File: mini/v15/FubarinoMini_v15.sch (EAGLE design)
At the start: 35 parts, among them IC1 MCP1702T-3302E/MB, J1 M20, J2 M20, Q1 8MHz, Q2 32.768 KHz, U1 PIC32MX250F128D_44VTLA_44

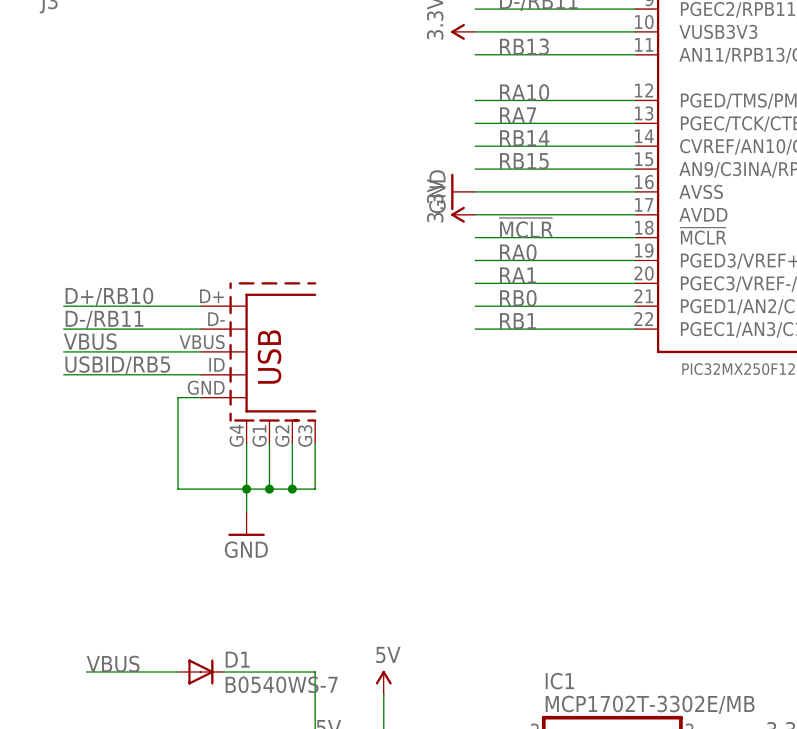
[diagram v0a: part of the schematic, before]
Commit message: "final" version 1.5 files, submitted to Microchip for their approval Updated USB connector footprint to Microchip's fav Hirose
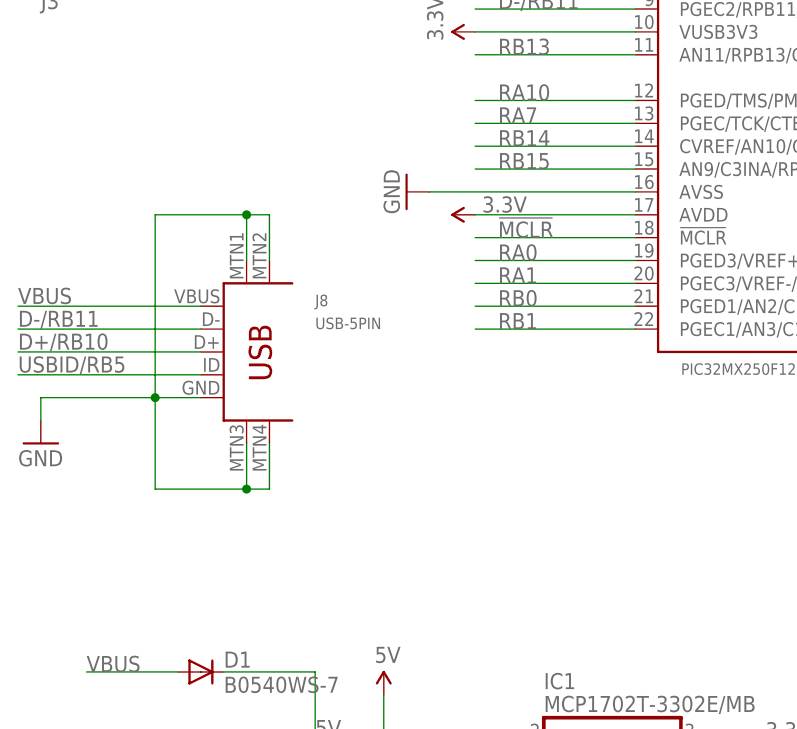
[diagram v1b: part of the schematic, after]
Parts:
- J8: value (none) -> USB-5PIN; device SparkFun02-20-08:USB_5PIN -> SchmalzHaus:USB-5PIN
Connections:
- net GND: now also J8.MTN1, J8.MTN2, J8.MTN3, J8.MTN4; no longer J8.P$1, J8.P$2, J8.P$3, J8.SHIELD
- net USBID/RB5: now also J8.ID; no longer J8.USB_ID
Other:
- note removed: "J8"
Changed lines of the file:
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@@
 <layer number="122" name="_bsilk" color="7" fill="1" visible="no" active="no"/>
 <layer number="125" name="_tNames" color="7" fill="1" visible="yes" active="yes"/>
+<layer number="128" name="128bmp" color="7" fill="1" visible="yes" active="yes"/>
+<layer number="129" name="129bmp" color="7" fill="1" visible="yes" active="yes"/>
+<layer number="130" name="130bmp" color="7" fill="1" visible="yes" active="yes"/>
 <layer number="144" name="Drill_legend" color="7" fill="1" visible="yes" active="yes"/>
 <layer number="151" name="HeatSink" color="7" fill="1" visible="no" active="no"/>
+<layer number="199" name="Contour" color="7" fill="1" visible="yes" active="yes"/>
 <layer number="200" name="200bmp" color="1" fill="10" visible="no" active="no"/>
 <layer number="201" name="201bmp" color="2" fill="1" visible="no" active="no"/>
@@
 <part name="GND8" library="SparkFun02-20-08" deviceset="GND" device=""/>
 <part name="FRAME2" library="SparkFun02-20-08" deviceset="FRAME-A3" device=""/>
-<part name="J8" library="SparkFun02-20-08" deviceset="USB_5PIN" device=""/>
 <part name="GND20" library="SparkFun02-20-08" deviceset="GND" device=""/>
 <part name="C13" library="SparkFun02-20-08" deviceset="CAP" device="0805" value="10uF"/>
@@
 <part name="U$3" library="SchmalzHausPublic" deviceset="ROSH_GARBAGE" device=""/>
 <part name="U$4" library="SchmalzHausPublic" deviceset="CHIPKIT" device="2MM"/>
+<part name="J8" library="SchmalzHaus" deviceset="USB-5PIN" device=""/>
 </parts>
 <sheets>
@@
 <plain>
 <text x="137.16" y="27.94" size="1.778" layer="98" rot="R90">Power ON LED</text>
-<text x="30.48" y="106.68" size="1.778" layer="98">USB Function (Mini B)</text>
+<text x="22.86" y="114.3" size="1.778" layer="98">USB Function (Mini B)</text>
 <text x="8.89" y="247.142" size="6.4516" layer="98" ratio="15">Fubarino Mini</text>
 <text x="88.646" y="247.65" size="6.4516" layer="98" ratio="15">www.fubarino.org/Mini</text>
 <text x="8.636" y="238.506" size="1.778" layer="98">By: Brian Schmalz and Rick Anderson</text>
 <text x="8.636" y="235.966" size="1.778" layer="98">licenced under Creative Commons v3.0 Attribution licence</text>
-<text x="48.26" y="96.52" size="1.778" layer="98">J8</text>
 <text x="8.128" y="231.394" size="1.778" layer="98">If you like the Fubarino, please consider that</text>
 <text x="8.128" y="228.854" size="1.778" layer="98">SchmalzHaus can design a customized version</text>
@@
 <instance part="LED2" gate="G$1" x="335.28" y="124.46" rot="R90"/>
 <instance part="GND19" gate="1" x="251.46" y="99.06"/>
-<instance part="GND2" gate="1" x="40.64" y="76.2"/>
+<instance part="GND2" gate="1" x="17.78" y="86.36"/>
 <instance part="P+3" gate="G$1" x="226.06" y="111.76" rot="R270"/>
 <instance part="P+15" gate="G$1" x="228.6" y="180.34"/>
@@
 <instance part="GND8" gate="1" x="111.76" y="25.4"/>
 <instance part="FRAME2" gate="G$1" x="0" y="0"/>
-<instance part="J8" gate="G$1" x="43.18" y="96.52" smashed="yes"/>
 <instance part="GND20" gate="1" x="55.88" y="25.4"/>
 <instance part="C13" gate="G$1" x="111.76" y="40.64"/>
@@
 <instance part="C15" gate="G$1" x="256.54" y="109.22" rot="R180"/>
 <instance part="P+2" gate="G$1" x="218.44" y="144.78" rot="R270"/>
-<instance part="P+6" gate="G$1" x="66.04" y="111.76" rot="R90"/>
+<instance part="P+6" gate="G$1" x="66.04" y="111.76" smashed="yes" rot="R90">
+<attribute name="VALUE" x="66.802" y="112.014" size="1.778" layer="96"/>
+</instance>
 <instance part="GND3" gate="1" x="63.5" y="142.24" rot="R270"/>
-<instance part="GND7" gate="1" x="63.5" y="114.3" rot="R270"/>
+<instance part="GND7" gate="1" x="58.42" y="114.3" rot="R270"/>
 <instance part="U$1" gate="G$1" x="276.86" y="10.16"/>
 <instance part="LOGO1" gate="G$1" x="256.54" y="12.7"/>
@@
 <instance part="U$3" gate="G$1" x="236.22" y="12.7"/>
 <instance part="U$4" gate="G$1" x="236.22" y="15.24"/>
+<instance part="J8" gate="G$1" x="40.64" y="96.52"/>
 </instances>
 <busses>
@@
 </segment>
 <segment>
-<wire x1="33.02" y1="91.44" x2="35.56" y2="91.44" width="0.1524" layer="91"/>
-<wire x1="33.02" y1="91.44" x2="33.02" y2="81.28" width="0.1524" layer="91"/>
-<wire x1="33.02" y1="81.28" x2="40.64" y2="81.28" width="0.1524" layer="91"/>
+<wire x1="35.56" y1="91.44" x2="30.48" y2="91.44" width="0.1524" layer="91"/>
+<wire x1="30.48" y1="91.44" x2="17.78" y2="91.44" width="0.1524" layer="91"/>
+<wire x1="17.78" y1="91.44" x2="17.78" y2="88.9" width="0.1524" layer="91"/>
+<pinref part="GND2" gate="1" pin="GND"/>
+<pinref part="J8" gate="G$1" pin="GND"/>
+<wire x1="30.48" y1="91.44" x2="30.48" y2="81.28" width="0.1524" layer="91"/>
+<junction x="30.48" y="91.44"/>
+<wire x1="30.48" y1="91.44" x2="30.48" y2="111.76" width="0.1524" layer="91"/>
+<pinref part="J8" gate="G$1" pin="MTN1"/>
+<wire x1="30.48" y1="111.76" x2="40.64" y2="111.76" width="0.1524" layer="91"/>
+<wire x1="40.64" y1="111.76" x2="40.64" y2="106.68" width="0.1524" layer="91"/>
+<pinref part="J8" gate="G$1" pin="MTN2"/>
+<wire x1="40.64" y1="111.76" x2="43.18" y2="111.76" width="0.1524" layer="91"/>
+<wire x1="43.18" y1="111.76" x2="43.18" y2="106.68" width="0.1524" layer="91"/>
+<junction x="40.64" y="111.76"/>
+<pinref part="J8" gate="G$1" pin="MTN3"/>
+<wire x1="30.48" y1="81.28" x2="40.64" y2="81.28" width="0.1524" layer="91"/>
 <wire x1="40.64" y1="81.28" x2="40.64" y2="86.36" width="0.1524" layer="91"/>
+<pinref part="J8" gate="G$1" pin="MTN4"/>
 <wire x1="40.64" y1="81.28" x2="43.18" y2="81.28" width="0.1524" layer="91"/>
 <wire x1="43.18" y1="81.28" x2="43.18" y2="86.36" width="0.1524" layer="91"/>
-<wire x1="43.18" y1="81.28" x2="45.72" y2="81.28" width="0.1524" layer="91"/>
-<wire x1="45.72" y1="81.28" x2="45.72" y2="86.36" width="0.1524" layer="91"/>
-<wire x1="45.72" y1="81.28" x2="48.26" y2="81.28" width="0.1524" layer="91"/>
-<wire x1="48.26" y1="81.28" x2="48.26" y2="86.36" width="0.1524" layer="91"/>
-<wire x1="40.64" y1="81.28" x2="40.64" y2="78.74" width="0.1524" layer="91"/>
 <junction x="40.64" y="81.28"/>
-<junction x="43.18" y="81.28"/>
-<junction x="45.72" y="81.28"/>
-<pinref part="J8" gate="G$1" pin="SHIELD"/>
-<pinref part="J8" gate="G$1" pin="P$1"/>
-<pinref part="J8" gate="G$1" pin="P$2"/>
-<pinref part="J8" gate="G$1" pin="P$3"/>
-<pinref part="J8" gate="G$1" pin="GND"/>
-<pinref part="GND2" gate="1" pin="GND"/>
 </segment>
 <segment>
@@
 </segment>
 <segment>
-<wire x1="83.82" y1="114.3" x2="66.04" y2="114.3" width="0.1524" layer="91"/>
+<wire x1="83.82" y1="114.3" x2="60.96" y2="114.3" width="0.1524" layer="91"/>
 <pinref part="GND7" gate="1" pin="GND"/>
 <pinref part="U1" gate="G$1" pin="AVSS"/>
@@
 <net name="D+/RB10" class="0">
 <segment>
-<wire x1="35.56" y1="101.6" x2="20.32" y2="101.6" width="0.1524" layer="91"/>
-<label x="20.32" y="101.854" size="1.778" layer="95"/>
+<label x="15.24" y="96.774" size="1.778" layer="95"/>
+<wire x1="15.24" y1="96.52" x2="35.56" y2="96.52" width="0.1524" layer="91"/>
 <pinref part="J8" gate="G$1" pin="D+"/>
 </segment>
@@
 <net name="D-/RB11" class="0">
 <segment>
-<wire x1="35.56" y1="99.06" x2="20.32" y2="99.06" width="0.1524" layer="91"/>
-<label x="20.32" y="99.314" size="1.778" layer="95"/>
+<label x="15.24" y="99.314" size="1.778" layer="95"/>
+<wire x1="15.24" y1="99.06" x2="35.56" y2="99.06" width="0.1524" layer="91"/>
 <pinref part="J8" gate="G$1" pin="D-"/>
 </segment>
@@
 <net name="USBID/RB5" class="0">
 <segment>
-<wire x1="35.56" y1="93.98" x2="20.32" y2="93.98" width="0.1524" layer="91"/>
-<label x="20.32" y="94.234" size="1.778" layer="95"/>
-<pinref part="J8" gate="G$1" pin="USB_ID"/>
+<label x="15.24" y="94.234" size="1.778" layer="95"/>
+<wire x1="35.56" y1="93.98" x2="15.24" y2="93.98" width="0.1524" layer="91"/>
+<pinref part="J8" gate="G$1" pin="ID"/>
 </segment>
 <segment>
@@
 <net name="VBUS" class="0">
 <segment>
-<wire x1="35.56" y1="96.52" x2="20.32" y2="96.52" width="0.1524" layer="91"/>
-<label x="20.32" y="96.774" size="1.778" layer="95"/>
+<label x="15.24" y="101.854" size="1.778" layer="95"/>
+<wire x1="35.56" y1="101.6" x2="15.24" y2="101.6" width="0.1524" layer="91"/>
 <pinref part="J8" gate="G$1" pin="VBUS"/>
 </segment>

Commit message: Added license text to schematic.
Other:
- note added: "Copyright 2012 Brian Schmalz Copyright and related rights are licensed under the Solderpad Hardware License, Version 0.51 (the “License”);"
- note added: "See the License for the specific language governing permissions and limitations under the License."
- note added: "software, hardware and materials distributed under this License is distributed on an “AS IS” BASIS, WITHOUT WARRANTIES OR CONDITIONS OF ANY KIND, either express or implied."
- note added: "you may not use this file except in compliance with the License. You may obtain a copy of the License at http://solderpad.org/licenses/SHL-0.51. Unless required by applicable law or agreed to in writing,"
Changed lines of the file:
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@@
 <text x="10.668" y="172.974" size="1.778" layer="98">Added CE, RoSH, and chipKIT graphics to silk on back</text>
 <text x="8.89" y="242.062" size="2.54" layer="98" ratio="15">A DIP form factor chipKIT® compatible board</text>
+<text x="5.08" y="12.7" size="1.778" layer="98">Copyright 2012 Brian Schmalz Copyright and related rights are licensed under the Solderpad Hardware License, Version 0.51 (the “License”); </text>
+<text x="5.08" y="10.16" size="1.778" layer="98">you may not use this file except in compliance with the License. You may obtain a copy of the License at http://solderpad.org/licenses/SHL-0.51. Unless required by applicable law or agreed to in writing,</text>
+<text x="5.08" y="7.62" size="1.778" layer="98"> software, hardware and materials distributed under this License is distributed on an “AS IS” BASIS, WITHOUT WARRANTIES OR CONDITIONS OF ANY KIND, either express or implied. </text>
+<text x="5.08" y="5.08" size="1.778" layer="98"> See the License for the specific language governing permissions and limitations under the License.</text>
 </plain>
 <instances>
